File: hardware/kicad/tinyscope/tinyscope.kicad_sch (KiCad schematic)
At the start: 0 parts

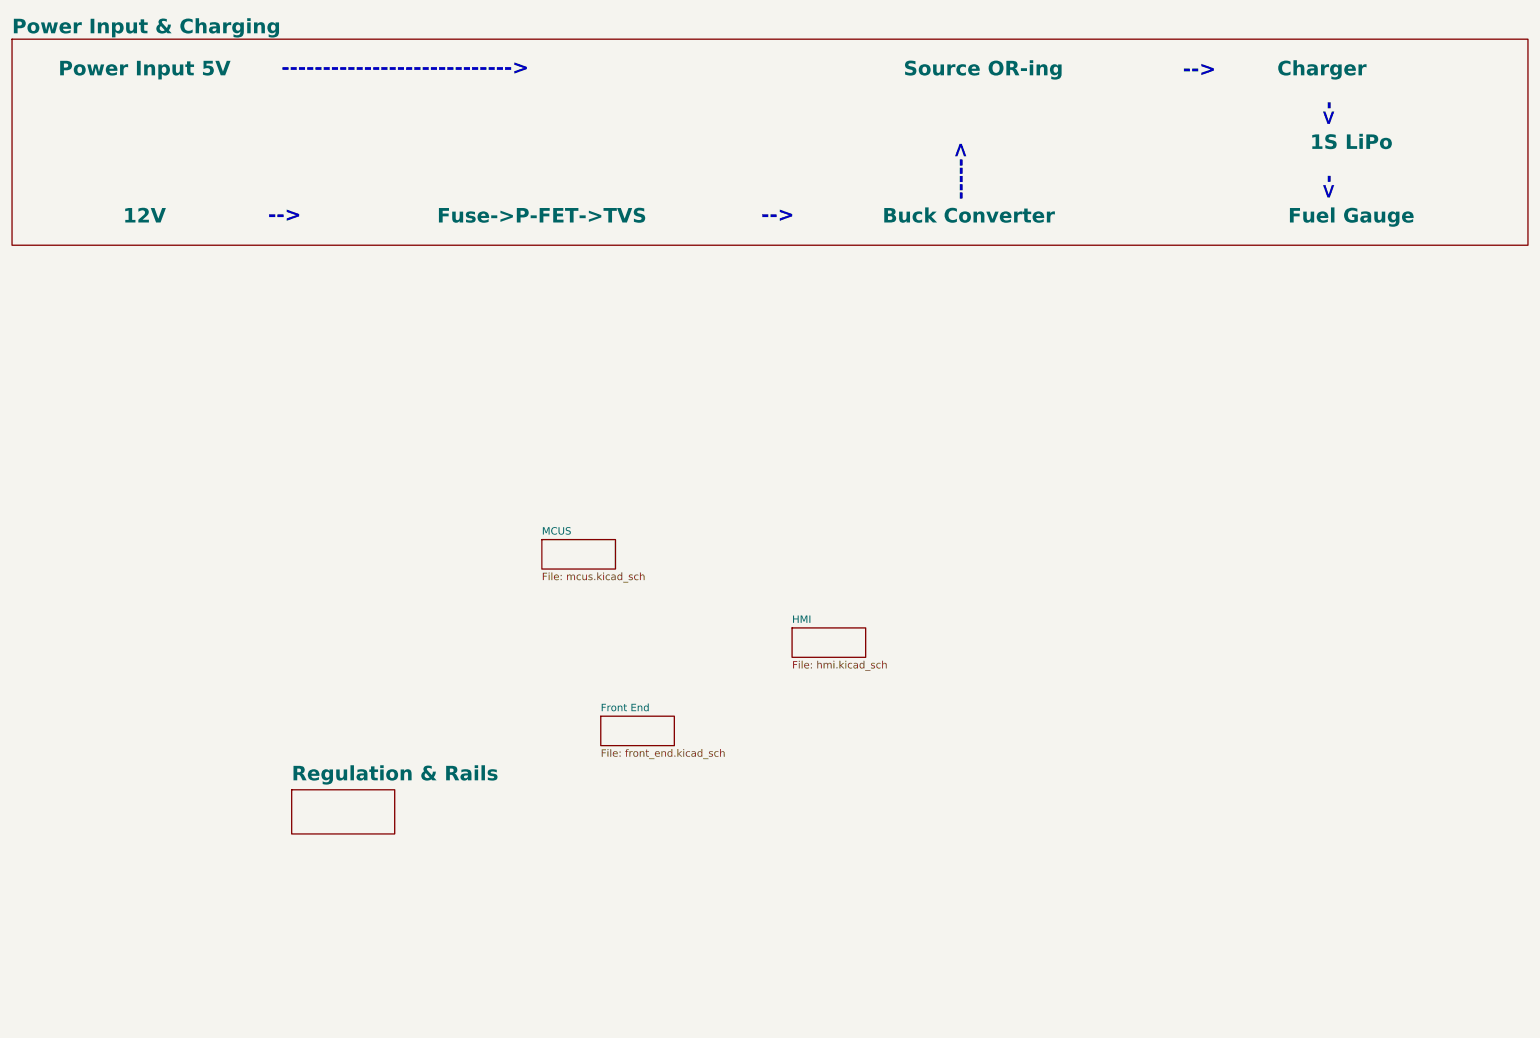
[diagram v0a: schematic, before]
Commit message: feat: hardware: Add tinyscope kicad project. Create flow diagram for Regulation & Rails schemat
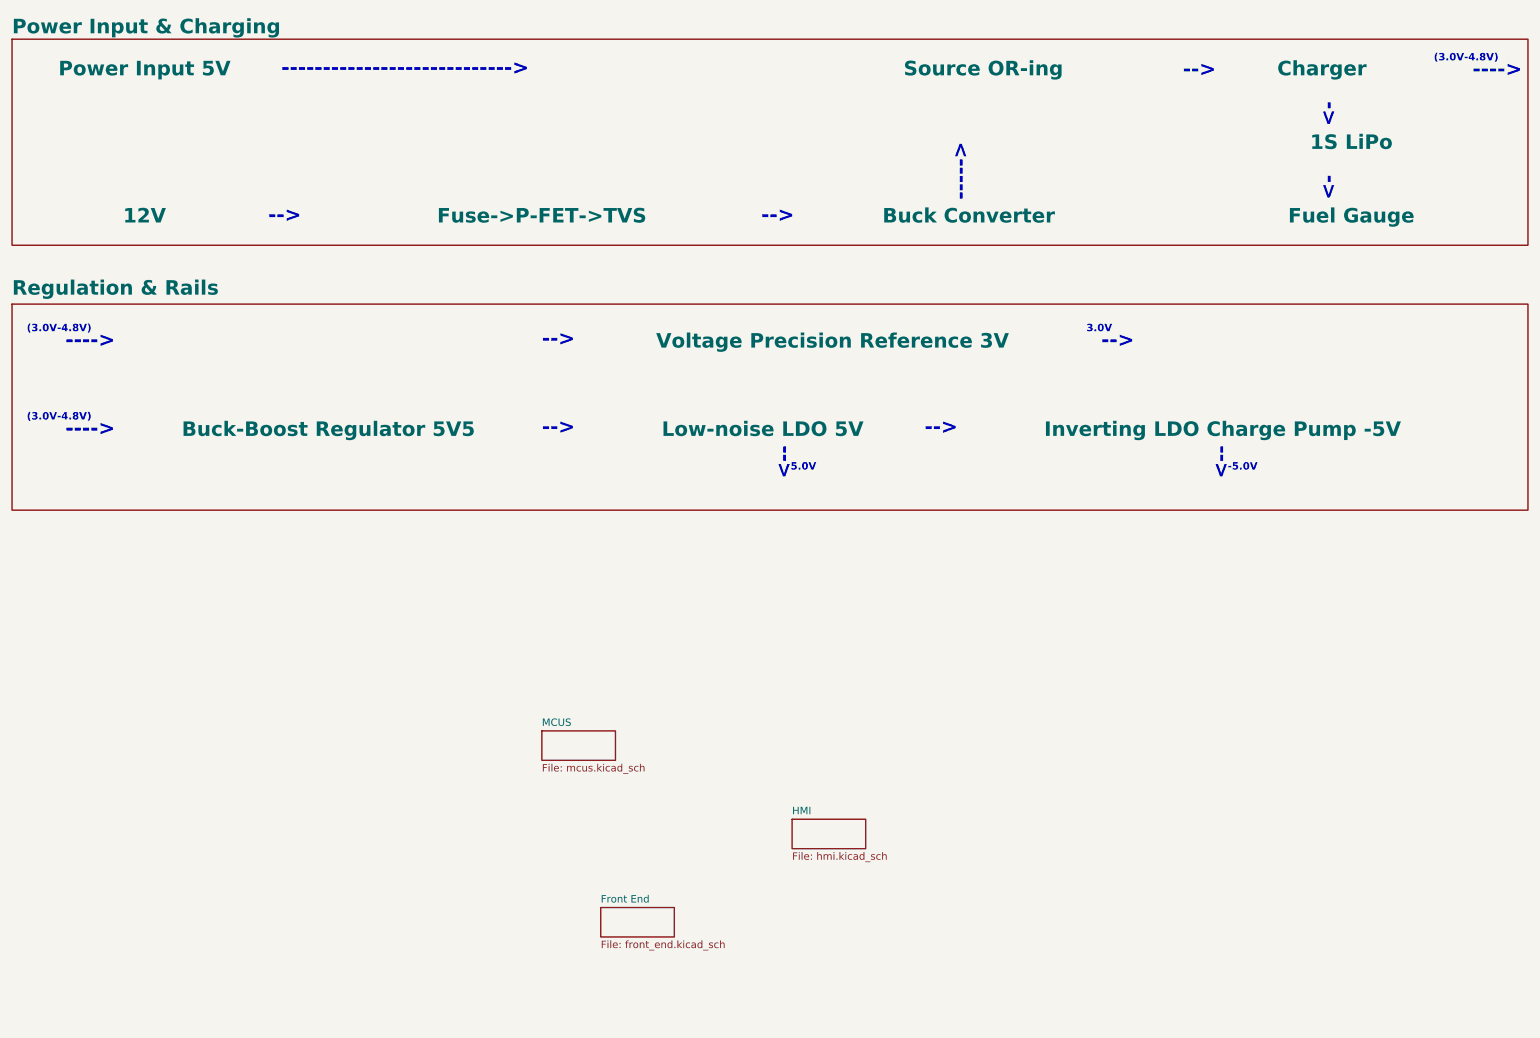
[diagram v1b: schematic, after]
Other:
- note added: "(3.0V-4.8V)"
- note added: "---->"
- note added: "-5.0V"
- note added: "3.0V"
- note added: "5.0V"
- note added: "<--"
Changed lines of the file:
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@@
     (rev "0.1")
+  )
+  (text "-->" (at 109.22 73.66 0)
+    (effects (font (size 2.5 2.5) (thickness 0.7) bold (color 0 0 0 1)) (justify left bottom))
+  )
+  (text "-->" (at 211.455 73.914 0)
+    (effects (font (size 2.5 2.5) (thickness 0.7) bold (color 255 0 0 1)) (justify right bottom))
+  )
+  (text "5.0V" (at 152.146 94.996 0)
+    (effects (font (size 1.27 1.27) (thickness 0.254) bold (color 255 0 0 1)) (justify left bottom))
   )
   (text "<-" (at 246.38 35.56 90)
     (effects (font (size 2.5 2.5) (thickness 0.7) bold (color 0 0 0 1)) (justify left bottom))
   )
+  (text "-5.0V" (at 227.584 94.996 0)
+    (effects (font (size 1.27 1.27) (thickness 0.254) bold (color 255 0 0 1)) (justify left bottom))
+  )
+  (text "<--" (at 227.838 90.678 90)
+    (effects (font (size 2.5 2.5) (thickness 0.7) bold (color 255 0 0 1)) (justify right bottom))
+  )
   (text "---------------------------->" (at 64.262 26.924 0)
     (effects (font (size 2.5 2.5) (thickness 0.7) bold (color 0 0 0 1)) (justify left bottom))
+  )
+  (text "<--" (at 152.4 90.678 90)
+    (effects (font (size 2.5 2.5) (thickness 0.7) bold (color 255 0 0 1)) (justify right bottom))
+  )
+  (text "(3.0V-4.8V)" (at 263.144 24.384 0)
+    (effects (font (size 1.27 1.27) (thickness 0.254) bold (color 255 0 0 1)) (justify left bottom))
   )
   (text "-->" (at 61.976 52.324 0)
@@
     (effects (font (size 2.5 2.5) (thickness 0.7) bold (color 0 0 0 1)) (justify right bottom))
   )
+  (text "-->" (at 109.22 88.9 0)
+    (effects (font (size 2.5 2.5) (thickness 0.7) bold (color 0 0 0 1)) (justify left bottom))
+  )
   (text "<-" (at 246.38 48.26 90)
     (effects (font (size 2.5 2.5) (thickness 0.7) bold (color 0 0 0 1)) (justify left bottom))
+  )
+  (text "---->" (at 35.56 89.154 0)
+    (effects (font (size 2.5 2.5) (thickness 0.7) bold (color 255 0 0 1)) (justify right bottom))
+  )
+  (text "(3.0V-4.8V)" (at 20.32 86.36 0)
+    (effects (font (size 1.27 1.27) (thickness 0.254) bold (color 255 0 0 1)) (justify left bottom))
   )
   (text "----->" (at 182.88 48.26 90)
     (effects (font (size 2.5 2.5) (thickness 0.7) bold (color 0 0 0 1)) (justify left bottom))
   )
+  (text "-->" (at 175.26 88.9 0)
+    (effects (font (size 2.5 2.5) (thickness 0.7) bold (color 0 0 0 1)) (justify left bottom))
+  )
+  (text "---->" (at 278.384 27.178 0)
+    (effects (font (size 2.5 2.5) (thickness 0.7) bold (color 255 0 0 1)) (justify right bottom))
+  )
+  (text "---->" (at 35.56 73.914 0)
+    (effects (font (size 2.5 2.5) (thickness 0.7) bold (color 255 0 0 1)) (justify right bottom))
+  )
   (text "-->" (at 147.066 52.324 0)
     (effects (font (size 2.5 2.5) (thickness 0.7) bold (color 0 0 0 1)) (justify left bottom))
   )
-  (sheet (at 66.04 149.86) (size 17.78 7.62) (fields_autoplaced)
+  (text "(3.0V-4.8V)" (at 20.32 71.12 0)
+    (effects (font (size 1.27 1.27) (thickness 0.254) bold (color 255 0 0 1)) (justify left bottom))
+  )
+  (text "3.0V" (at 203.2 71.12 0)
+    (effects (font (size 1.27 1.27) (thickness 0.254) bold (color 255 0 0 1)) (justify left bottom))
+  )
+  (sheet (at 17.78 66.04) (size 261.62 35.56)
     (stroke (width 0.1524) (type solid))
-    (fill (color 0 0 0 0.0000))
-    (property "Sheetname" "Regulation & Rails" (at 66.04 148.5334 0)
+    (fill (color 255 255 194 1.0000))
+    (property "Sheetname" "Regulation & Rails" (at 17.78 64.7134 0)
       (effects (font (size 2.5 2.5) bold) (justify left bottom))
     )
-    (property "Sheetfile" "regulation_and_rails.kicad_sch" (at 66.04 158.0646 0)
+    (property "Sheetfile" "regulation_and_rails.kicad_sch" (at 17.78 94.5646 0)
       (effects (font (size 1.27 1.27)) (justify left top) hide)
+    )
+    (property "TPS63802" "Buck-Boost Regulator 3V3" (at 72.39 72.39 0) (show_name)
+      (effects (font (size 2.5 2.5) bold))
+    )
+    (property "TPS63802" "Buck-Boost Regulator 5V5" (at 72.39 87.63 0) (show_name)
+      (effects (font (size 2.5 2.5) bold))
+    )
+    (property "ADP7142" "Low-noise LDO 5V" (at 147.32 87.63 0) (show_name)
+      (effects (font (size 2.5 2.5) bold))
+    )
+    (property "LM27761" "Inverting LDO Charge Pump -5V" (at 226.695 87.63 0) (show_name)
+      (effects (font (size 2.5 2.5) bold))
+    )
+    (property "REF3030" "Voltage Precision Reference 3V" (at 159.385 72.39 0) (show_name)
+      (effects (font (size 2.5 2.5) bold))
     )
     (instances
@@
     )
   )
-  (sheet (at 119.38 137.16) (size 12.7 5.08) (fields_autoplaced)
+  (sheet (at 119.38 170.18) (size 12.7 5.08) (fields_autoplaced)
     (stroke (width 0.1524) (type solid))
     (fill (color 255 255 194 1.0000))
-    (property "Sheetname" "Front End" (at 119.38 136.4484 0)
+    (property "Sheetname" "Front End" (at 119.38 169.4684 0)
       (effects (font (size 1.27 1.27)) (justify left bottom))
     )
-    (property "Sheetfile" "front_end.kicad_sch" (at 119.38 142.8246 0)
+    (property "Sheetfile" "front_end.kicad_sch" (at 119.38 175.8446 0)
       (effects (font (size 1.27 1.27)) (justify left top))
     )
@@
     )
   )
-  (sheet (at 152.4 121.92) (size 12.7 5.08) (fields_autoplaced)
+  (sheet (at 152.4 154.94) (size 12.7 5.08) (fields_autoplaced)
     (stroke (width 0.1524) (type solid))
     (fill (color 255 255 194 1.0000))
-    (property "Sheetname" "HMI" (at 152.4 121.2084 0)
+    (property "Sheetname" "HMI" (at 152.4 154.2284 0)
       (effects (font (size 1.27 1.27)) (justify left bottom))
     )
-    (property "Sheetfile" "hmi.kicad_sch" (at 152.4 127.5846 0)
+    (property "Sheetfile" "hmi.kicad_sch" (at 152.4 160.6046 0)
       (effects (font (size 1.27 1.27)) (justify left top))
     )
@@
     )
   )
-  (sheet (at 109.22 106.68) (size 12.7 5.08) (fields_autoplaced)
+  (sheet (at 109.22 139.7) (size 12.7 5.08) (fields_autoplaced)
     (stroke (width 0.1524) (type solid))
     (fill (color 0 0 0 0.0000))
-    (property "Sheetname" "MCUS" (at 109.22 105.9684 0)
+    (property "Sheetname" "MCUS" (at 109.22 138.9884 0)
       (effects (font (size 1.27 1.27)) (justify left bottom))
     )
-    (property "Sheetfile" "mcus.kicad_sch" (at 109.22 112.3446 0)
+    (property "Sheetfile" "mcus.kicad_sch" (at 109.22 145.3646 0)
       (effects (font (size 1.27 1.27)) (justify left top))
     )

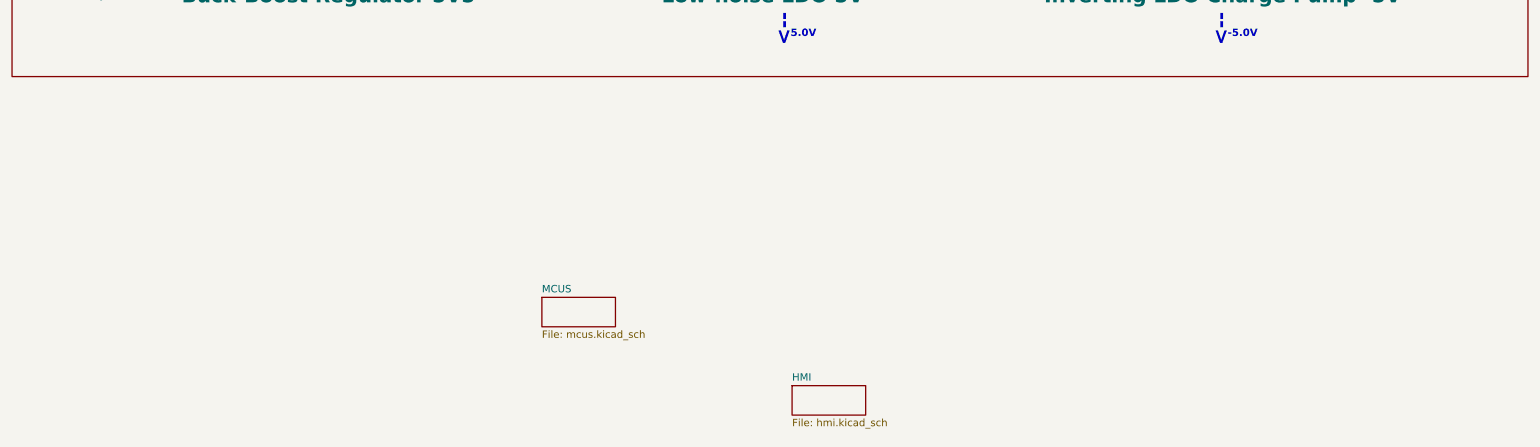
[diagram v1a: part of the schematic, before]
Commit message: feat: hardware: Add tinyscope kicad project. Create flow diagram for MCUs sheet. Adds decoupling caps for STM32H743
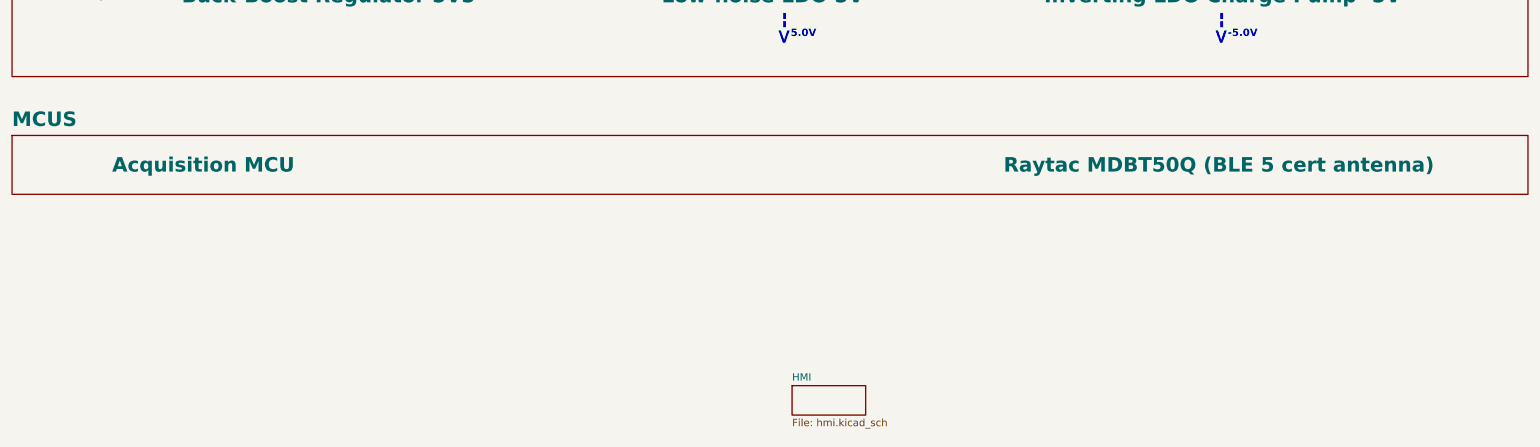
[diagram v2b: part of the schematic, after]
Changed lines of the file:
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@@
     (title "tinyscope")
     (date "2026-05-31")
-    (rev "0.1")
+    (rev "v0.1")
   )
   (text "-->" (at 109.22 73.66 0)
@@
     (instances
       (project "tinyscope"
-        (path "/bb072e32-cc57-415a-8554-0e84d374f333" (page "4"))
+        (path "/bb072e32-cc57-415a-8554-0e84d374f333" (page "3"))
       )
     )
@@
     (instances
       (project "tinyscope"
-        (path "/bb072e32-cc57-415a-8554-0e84d374f333" (page "3"))
+        (path "/bb072e32-cc57-415a-8554-0e84d374f333" (page "2"))
       )
     )
@@
     )
   )
-  (sheet (at 109.22 139.7) (size 12.7 5.08) (fields_autoplaced)
+  (sheet (at 17.78 111.76) (size 261.62 10.16)
     (stroke (width 0.1524) (type solid))
-    (fill (color 0 0 0 0.0000))
-    (property "Sheetname" "MCUS" (at 109.22 138.9884 0)
-      (effects (font (size 1.27 1.27)) (justify left bottom))
+    (fill (color 255 255 194 1.0000))
+    (property "Sheetname" "MCUS" (at 17.78 110.4334 0)
+      (effects (font (size 2.5 2.5) bold) (justify left bottom))
     )
-    (property "Sheetfile" "mcus.kicad_sch" (at 109.22 145.3646 0)
-      (effects (font (size 1.27 1.27)) (justify left top))
+    (property "Sheetfile" "mcus.kicad_sch" (at 17.78 135.2046 0)
+      (effects (font (size 1.27 1.27)) (justify left top) hide)
+    )
+    (property "STM32H743" "Acquisition MCU" (at 50.8 116.84 0) (show_name)
+      (effects (font (size 2.5 2.5) bold))
+    )
+    (property "nRF52840" "Raytac MDBT50Q (BLE 5 cert antenna)" (at 226.06 116.84 0) (show_name)
+      (effects (font (size 2.5 2.5) bold))
     )
     (instances
       (project "tinyscope"
-        (path "/bb072e32-cc57-415a-8554-0e84d374f333" (page "2"))
+        (path "/bb072e32-cc57-415a-8554-0e84d374f333" (page "4"))
       )
     )
